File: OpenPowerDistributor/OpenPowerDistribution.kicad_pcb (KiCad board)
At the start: 2 copper layers, 16 parts, among them U1 AP63200WU, U2 LGS6302

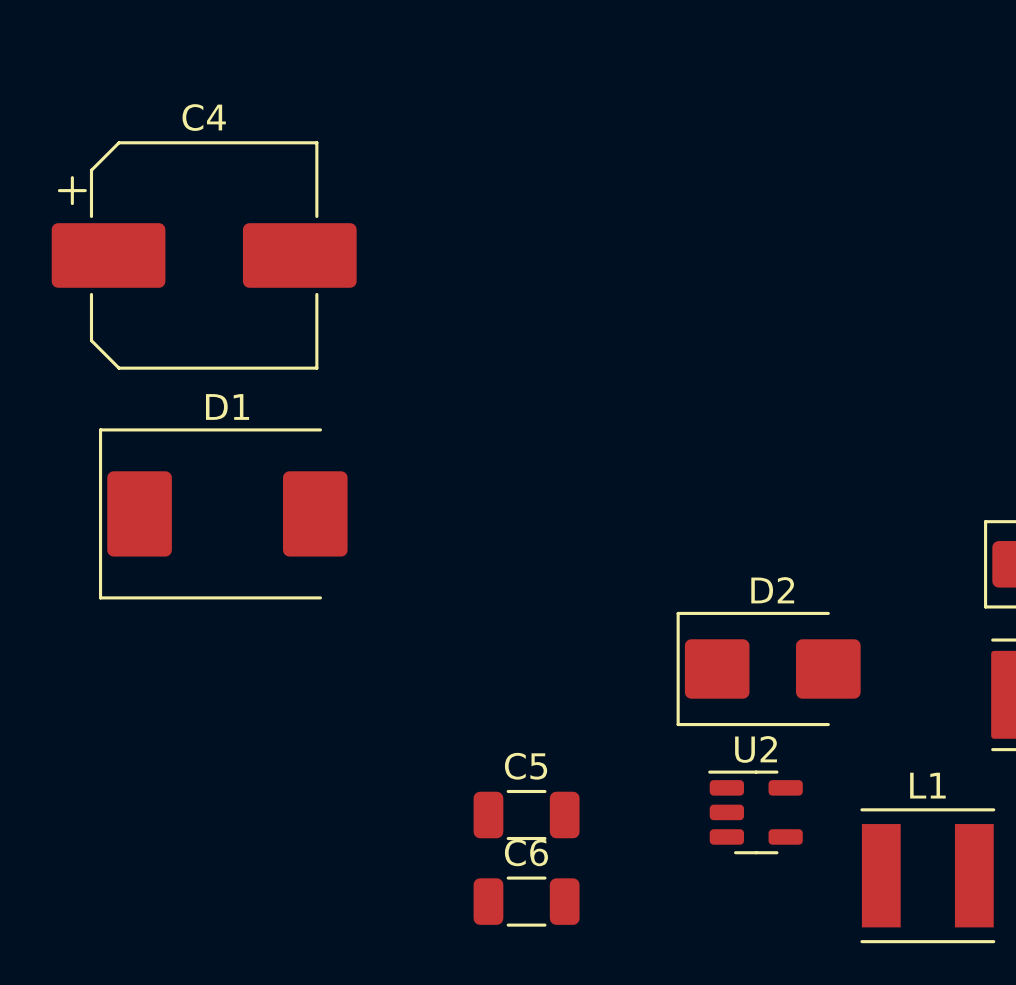
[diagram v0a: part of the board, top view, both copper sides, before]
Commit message: Added manual high side power switch
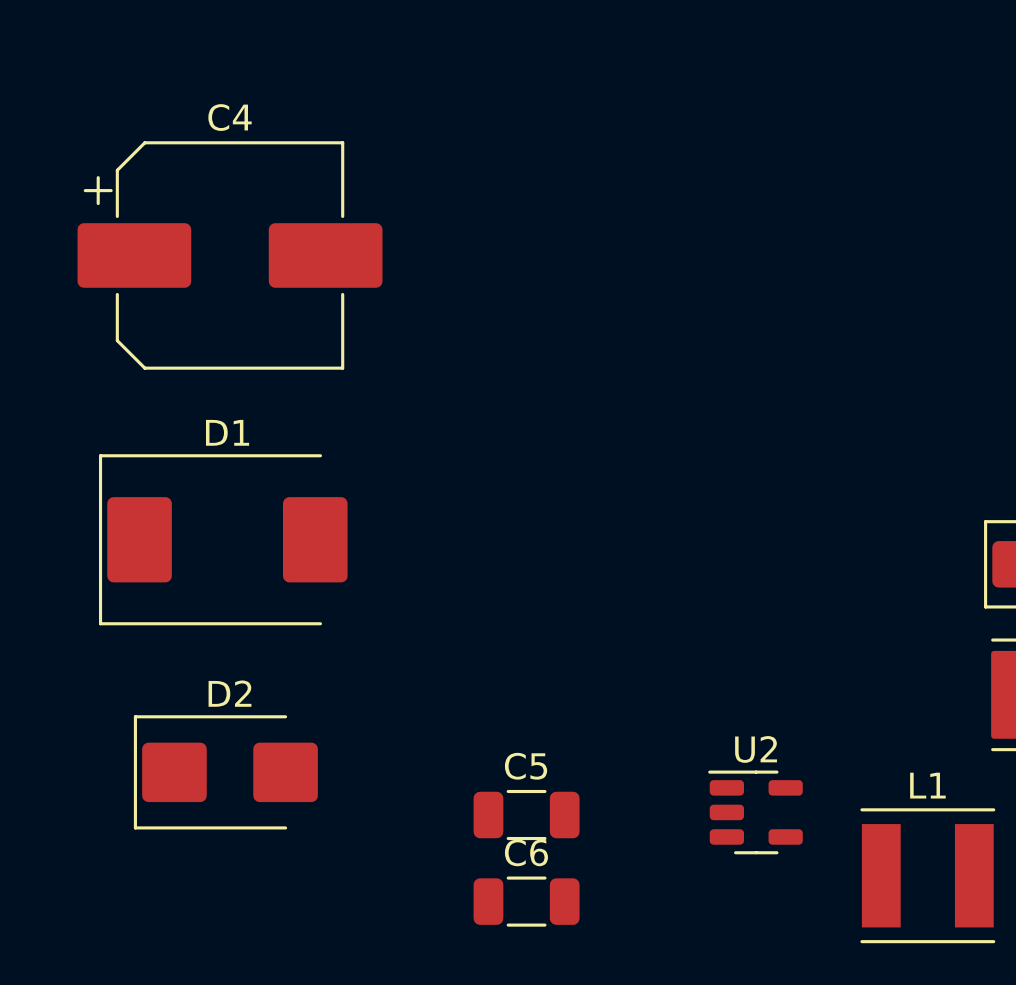
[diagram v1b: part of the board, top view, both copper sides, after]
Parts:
- moved D2 21.4 mm to (46.0, 60.0)
- moved C4 1.00 mm to (46.0, 40.0)
- moved D1 1.00 mm to (45.9, 51.0)
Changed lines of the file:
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@@
   (net 11 "+5V")
   (footprint "Diode_SMD:D_SMB" (layer "F.Cu")
-    (at 67 56)
+    (at 46 60)
     (descr "Diode SMB (DO-214AA)")
     (tags "Diode SMB (DO-214AA)")
@@
   )
   (footprint "Capacitor_SMD:CP_Elec_8x10.5" (layer "F.Cu")
-    (at 45 40)
+    (at 46 40)
     (descr "SMD capacitor, aluminum electrolytic, Vishay 0810, 8.0x10.5mm, http://www.vishay.com/docs/28395/150crz.pdf")
     (tags "capacitor electrolytic")
@@
   )
   (footprint "Diode_SMD:D_SMC" (layer "F.Cu")
-    (at 45.9 50)
+    (at 45.9 51)
     (descr "Diode SMC (DO-214AB)")
     (tags "Diode SMC (DO-214AB)")

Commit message: More schematic progress
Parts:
- added C10: 100nF 16V, Capacitor_SMD:C_0603_1608Metric, F.Cu at (-26.2, -64.5)
- added C11: 100nF 16V, Capacitor_SMD:C_0603_1608Metric, F.Cu at (-60.4, -53.8)
- added C12: NA, Capacitor_SMD:C_0603_1608Metric, F.Cu at (-60.4, -51.2)
- added C13: 100nF 16V, Capacitor_SMD:C_0603_1608Metric, F.Cu at (432.4, 46.4)
- added C14: 100nF 16V, Capacitor_SMD:C_0603_1608Metric, F.Cu at (432.4, 48.9)
- added C15: NA, Capacitor_SMD:C_0603_1608Metric, F.Cu at (432.4, 51.4)
- added C16: NA, Capacitor_SMD:C_0603_1608Metric, F.Cu at (432.4, 53.9)
- added C17: 100nF 16V, Capacitor_SMD:C_0603_1608Metric, F.Cu at (432.4, 56.4)
- added C18: 100nF 16V, Capacitor_SMD:C_0603_1608Metric, F.Cu at (468.5, 6.00)
- added C19: 100nF 16V, Capacitor_SMD:C_0603_1608Metric, F.Cu at (468.5, 8.51)
- added C20: NA, Capacitor_SMD:C_0603_1608Metric, F.Cu at (468.5, 11.0)
- added C21: NA, Capacitor_SMD:C_0603_1608Metric, F.Cu at (468.5, 13.5)
- added C22: 100nF 16V, Capacitor_SMD:C_0603_1608Metric, F.Cu at (468.5, 16.0)
- added C23: 100nF 16V, Capacitor_SMD:C_0603_1608Metric, F.Cu at (432.4, 6.00)
- added C24: 100nF 16V, Capacitor_SMD:C_0603_1608Metric, F.Cu at (432.4, 8.51)
- added C25: NA, Capacitor_SMD:C_0603_1608Metric, F.Cu at (432.4, 11.0)
- added C26: NA, Capacitor_SMD:C_0603_1608Metric, F.Cu at (432.4, 13.5)
- added C27: 100nF 16V, Capacitor_SMD:C_0603_1608Metric, F.Cu at (432.4, 16.0)
- added C28: 100nF 16V, Capacitor_SMD:C_0603_1608Metric, F.Cu at (391.6, 69.0)
- added C29: 100nF 16V, Capacitor_SMD:C_0603_1608Metric, F.Cu at (391.6, 71.5)
- added C30: NA, Capacitor_SMD:C_0603_1608Metric, F.Cu at (391.6, 74.0)
- added C31: NA, Capacitor_SMD:C_0603_1608Metric, F.Cu at (391.6, 76.5)
- added C32: 100nF 16V, Capacitor_SMD:C_0603_1608Metric, F.Cu at (391.6, 79.1)
- added C33: 100nF 16V, Capacitor_SMD:C_0603_1608Metric, F.Cu at (391.6, 25.6)
- added C34: 100nF 16V, Capacitor_SMD:C_0603_1608Metric, F.Cu at (391.6, 28.2)
- added C35: NA, Capacitor_SMD:C_0603_1608Metric, F.Cu at (391.6, 30.7)
- added C36: NA, Capacitor_SMD:C_0603_1608Metric, F.Cu at (391.6, 33.2)
- added C37: 100nF 16V, Capacitor_SMD:C_0603_1608Metric, F.Cu at (391.6, 35.7)
- added C38: 100nF 16V, Capacitor_SMD:C_0603_1608Metric, F.Cu at (432.4, 86.8)
- added C39: 100nF 16V, Capacitor_SMD:C_0603_1608Metric, F.Cu at (432.4, 89.3)
- added C40: NA, Capacitor_SMD:C_0603_1608Metric, F.Cu at (432.4, 91.8)
- added C41: NA, Capacitor_SMD:C_0603_1608Metric, F.Cu at (432.4, 94.3)
- added C42: 100nF 16V, Capacitor_SMD:C_0603_1608Metric, F.Cu at (432.4, 96.8)
- added C43: 100nF 16V, Capacitor_SMD:C_0603_1608Metric, F.Cu at (468.5, 46.4)
- added C44: 100nF 16V, Capacitor_SMD:C_0603_1608Metric, F.Cu at (468.5, 48.9)
- added C45: NA, Capacitor_SMD:C_0603_1608Metric, F.Cu at (468.5, 51.4)
- added C46: NA, Capacitor_SMD:C_0603_1608Metric, F.Cu at (468.5, 53.9)
- added C47: 100nF 16V, Capacitor_SMD:C_0603_1608Metric, F.Cu at (468.5, 56.4)
- added C48: 100nF 16V, Capacitor_SMD:C_0603_1608Metric, F.Cu at (391.6, 92.7)
- added C49: 100nF 16V, Capacitor_SMD:C_0603_1608Metric, F.Cu at (391.6, 95.2)
- added C50: NA, Capacitor_SMD:C_0603_1608Metric, F.Cu at (391.6, 97.8)
- added C51: NA, Capacitor_SMD:C_0603_1608Metric, F.Cu at (391.6, 100.3)
- added C52: 100nF 16V, Capacitor_SMD:C_0603_1608Metric, F.Cu at (391.6, 102.8)
- added C53: 10uF 50V, Capacitor_SMD:C_1206_3216Metric, F.Cu at (492.0, 14.6)
- added C54: 100nF 16V, Capacitor_SMD:C_0603_1608Metric, F.Cu at (492.6, 10.2)
- added C55: 47uF 16V, Capacitor_SMD:C_1210_3225Metric, F.Cu at (493.4, 6.87)
- added C57: 47uF 16V, Capacitor_SMD:C_1210_3225Metric, F.Cu at (473.7, 127.5)
- added C58: 100nF 16V, Capacitor_SMD:C_0603_1608Metric, F.Cu at (492.6, 26.9)
- added C59: 47uF 16V, Capacitor_SMD:C_1210_3225Metric, F.Cu at (493.4, 23.6)
- added C7: NA, Capacitor_SMD:C_0603_1608Metric, F.Cu at (125.5, 105.5)
- added C8: NA, Capacitor_SMD:C_0603_1608Metric, F.Cu at (-23.9, -59.7)
- added C9: 100nF 16V, Capacitor_SMD:C_0603_1608Metric, F.Cu at (118.7, 83.0)
- added D10: SS36(F), Diode_SMD:D_SMA, F.Cu at (-46.3, -42.6)
- added D11: SMAJ24A, Diode_SMD:D_SMA, F.Cu at (448.6, 96.9)
- added D12: SMAJ12A, Diode_SMD:D_SMA, F.Cu at (448.6, 101.4)
- added D13: SMAJ12A, Diode_SMD:D_SMA, F.Cu at (448.6, 106.0)
- added D14: AZ23C16, Package_TO_SOT_SMD:SOT-23, F.Cu at (428.0, 47.4)
- added D15: AZ23C16, Package_TO_SOT_SMD:SOT-23, F.Cu at (428.0, 51.8)
- added D16: SMAJ9.0A, Diode_SMD:D_SMA, F.Cu at (448.6, 110.5)
- added D17: SS36(F), Diode_SMD:D_SMA, F.Cu at (412.5, 72.7)
- added D18: SS36(F), Diode_SMD:D_SMA, F.Cu at (412.5, 77.2)
- added D19: SMAJ12A, Diode_SMD:D_SMA, F.Cu at (448.6, 115.1)
- added D20: SMAJ12A, Diode_SMD:D_SMA, F.Cu at (456.7, 87.8)
- added D21: AZ23C16, Package_TO_SOT_SMD:SOT-23, F.Cu at (464.1, 6.96)
- added D22: AZ23C16, Package_TO_SOT_SMD:SOT-23, F.Cu at (464.1, 11.4)
- added D23: SMAJ9.0A, Diode_SMD:D_SMA, F.Cu at (456.7, 92.3)
- added D24: SS36(F), Diode_SMD:D_SMA, F.Cu at (448.6, 32.3)
- added D25: SS36(F), Diode_SMD:D_SMA, F.Cu at (448.6, 36.8)
- added D26: SMAJ12A, Diode_SMD:D_SMA, F.Cu at (456.7, 96.9)
- added D27: SMAJ12A, Diode_SMD:D_SMA, F.Cu at (456.7, 101.4)
- added D28: AZ23C16, Package_TO_SOT_SMD:SOT-23, F.Cu at (428.0, 6.96)
- added D29: AZ23C16, Package_TO_SOT_SMD:SOT-23, F.Cu at (428.0, 11.4)
- added D30: SMAJ9.0A, Diode_SMD:D_SMA, F.Cu at (456.7, 106.0)
- added D31: SS36(F), Diode_SMD:D_SMA, F.Cu at (412.5, 32.3)
- added D32: SS36(F), Diode_SMD:D_SMA, F.Cu at (412.5, 36.8)
- added D33: SMAJ5.0A, Diode_SMD:D_SMA, F.Cu at (456.7, 110.5)
- added D34: SMAJ5.0A, Diode_SMD:D_SMA, F.Cu at (456.7, 115.1)
- added D35: SMAJ5.0A, Diode_SMD:D_SMA, F.Cu at (464.8, 87.8)
- added D36: SMAJ5.0A, Diode_SMD:D_SMA, F.Cu at (464.8, 92.3)
- added D37: SMAJ5.0A, Diode_SMD:D_SMA, F.Cu at (464.8, 96.9)
- added D38: SMAJ5.0A, Diode_SMD:D_SMA, F.Cu at (464.8, 101.4)
- added D39: AZ23C16, Package_TO_SOT_SMD:SOT-23, F.Cu at (370.1, 50.3)
- added D40: AZ23C16, Package_TO_SOT_SMD:SOT-23, F.Cu at (370.1, 54.8)
- added D41: AZ23C16, Package_TO_SOT_SMD:SOT-23, F.Cu at (447.0, 47.4)
- added D42: SS36(F), Diode_SMD:D_SMA, F.Cu at (402.5, 50.4)
- added D43: SS36(F), Diode_SMD:D_SMA, F.Cu at (402.5, 54.9)
- added D44: AZ23C16, Package_TO_SOT_SMD:SOT-23, F.Cu at (370.1, 6.96)
- added D45: AZ23C16, Package_TO_SOT_SMD:SOT-23, F.Cu at (370.1, 11.4)
- added D46: AZ23C16, Package_TO_SOT_SMD:SOT-23, F.Cu at (447.0, 51.8)
- added D47: SS36(F), Diode_SMD:D_SMA, F.Cu at (402.5, 7.01)
- added D48: SS36(F), Diode_SMD:D_SMA, F.Cu at (402.5, 11.6)
- added D49: AZ23C16, Package_TO_SOT_SMD:SOT-23, F.Cu at (428.0, 87.8)
- added D5: SS36(F), Diode_SMD:D_SMA, F.Cu at (-26.1, -80.0)
- added D50: AZ23C16, Package_TO_SOT_SMD:SOT-23, F.Cu at (428.0, 92.2)
- added D51: SS36(F), Diode_SMD:D_SMA, F.Cu at (462.3, 72.7)
- added D52: SS36(F), Diode_SMD:D_SMA, F.Cu at (412.5, 113.1)
- added D53: SS36(F), Diode_SMD:D_SMA, F.Cu at (412.5, 117.6)
- added D54: SS36(F), Diode_SMD:D_SMA, F.Cu at (462.3, 77.2)
- added D55: AZ23C16, Package_TO_SOT_SMD:SOT-23, F.Cu at (387.2, 93.7)
- added D56: AZ23C16, Package_TO_SOT_SMD:SOT-23, F.Cu at (387.2, 98.2)
- added D57: SS36(F), Diode_SMD:D_SMA, F.Cu at (371.8, 119.0)
- added D58: SS36(F), Diode_SMD:D_SMA, F.Cu at (371.8, 123.6)
- added D6: AZ23C16, Package_TO_SOT_SMD:SOT-23, F.Cu at (490.3, 87.7)
- added D7: SMAJ24A, Diode_SMD:D_SMA, F.Cu at (448.6, 87.8)
- added D8: AZ23C16, Package_TO_SOT_SMD:SOT-23, F.Cu at (-31.9, -80.0)
- added D9: SMAJ9.0A, Diode_SMD:D_SMA, F.Cu at (448.6, 92.3)
- added J1: Barrel_Jack, Connector_BarrelJack:BarrelJack_Horizontal, F.Cu at (485.4, 118.1)
- added J10: Barrel_Jack, Connector_BarrelJack:BarrelJack_Horizontal, F.Cu at (387.1, 53.5)
- added J11: Barrel_Jack, Connector_BarrelJack:BarrelJack_Horizontal, F.Cu at (387.1, 66.1)
- added J12: Barrel_Jack, Connector_BarrelJack:BarrelJack_Horizontal, F.Cu at (387.1, 10.1)
- added J13: Barrel_Jack, Connector_BarrelJack:BarrelJack_Horizontal, F.Cu at (387.1, 22.7)
- added J14: Barrel_Jack, Connector_BarrelJack:BarrelJack_Horizontal, F.Cu at (423.0, 90.9)
- added J15: Barrel_Jack, Connector_BarrelJack:BarrelJack_Horizontal, F.Cu at (423.0, 103.5)
- added J16: Barrel_Jack, Connector_BarrelJack:BarrelJack_Horizontal, F.Cu at (464.0, 50.5)
- added J17: Barrel_Jack, Connector_BarrelJack:BarrelJack_Horizontal, F.Cu at (464.0, 63.1)
- added J18: Barrel_Jack, Connector_BarrelJack:BarrelJack_Horizontal, F.Cu at (382.2, 96.8)
- added J19: Barrel_Jack, Connector_BarrelJack:BarrelJack_Horizontal, F.Cu at (382.2, 109.5)
- added J2: Barrel_Jack, Connector_BarrelJack:BarrelJack_Horizontal, F.Cu at (-36.5, -75.2)
- added J3: Barrel_Jack, Connector_BarrelJack:BarrelJack_Horizontal, F.Cu at (485.4, 103.5)
- added J4: Barrel_Jack, Connector_BarrelJack:BarrelJack_Horizontal, F.Cu at (423.0, 50.5)
- added J5: Barrel_Jack, Connector_BarrelJack:BarrelJack_Horizontal, F.Cu at (423.0, 63.1)
- added J6: Barrel_Jack, Connector_BarrelJack:BarrelJack_Horizontal, F.Cu at (459.1, 10.1)
- added J7: Barrel_Jack, Connector_BarrelJack:BarrelJack_Horizontal, F.Cu at (459.1, 22.7)
- added J8: Barrel_Jack, Connector_BarrelJack:BarrelJack_Horizontal, F.Cu at (423.0, 10.1)
- added J9: Barrel_Jack, Connector_BarrelJack:BarrelJack_Horizontal, F.Cu at (423.0, 22.7)
- added L3: 3.3uH, Inductor_SMD:L_Bourns_SRP7028A_7.3x6.6mm, F.Cu at (485.6, 8.81)
- added L4: 3.3uH, Inductor_SMD:L_Bourns_SRP7028A_7.3x6.6mm, F.Cu at (485.6, 25.5)
- added Q1: STN2610D, Package_TO_SOT_SMD:TO-252-2, F.Cu at (-26.2, -74.5)
- added Q10: BC847, Package_TO_SOT_SMD:SOT-23, F.Cu at (428.0, 69.6)
- added Q11: STN2610D, Package_TO_SOT_SMD:TO-252-2, F.Cu at (437.3, 66.7)
- added Q12: STN2610D, Package_TO_SOT_SMD:TO-252-2, F.Cu at (437.3, 74.8)
- added Q13: BC847, Package_TO_SOT_SMD:SOT-23, F.Cu at (464.1, 15.9)
- added Q14: BC847, Package_TO_SOT_SMD:SOT-23, F.Cu at (464.1, 20.3)
- added Q15: BC847, Package_TO_SOT_SMD:SOT-23, F.Cu at (464.1, 24.8)
- added Q16: BC847, Package_TO_SOT_SMD:SOT-23, F.Cu at (464.1, 29.2)
- added Q17: STN2610D, Package_TO_SOT_SMD:TO-252-2, F.Cu at (473.4, 26.3)
- added Q18: STN2610D, Package_TO_SOT_SMD:TO-252-2, F.Cu at (473.4, 34.4)
- added Q19: BC847, Package_TO_SOT_SMD:SOT-23, F.Cu at (428.0, 15.9)
- added Q2: BC847, Package_TO_SOT_SMD:SOT-23, F.Cu at (-30.6, -61.3)
- added Q20: BC847, Package_TO_SOT_SMD:SOT-23, F.Cu at (428.0, 20.3)
- added Q21: BC847, Package_TO_SOT_SMD:SOT-23, F.Cu at (428.0, 24.8)
- added Q22: BC847, Package_TO_SOT_SMD:SOT-23, F.Cu at (428.0, 29.2)
- added Q23: STN2610D, Package_TO_SOT_SMD:TO-252-2, F.Cu at (437.3, 26.3)
- added Q24: STN2610D, Package_TO_SOT_SMD:TO-252-2, F.Cu at (437.3, 34.4)
- added Q25: BC847, Package_TO_SOT_SMD:SOT-23, F.Cu at (370.1, 59.2)
- added Q26: BC847, Package_TO_SOT_SMD:SOT-23, F.Cu at (370.1, 63.7)
- added Q27: BC847, Package_TO_SOT_SMD:SOT-23, F.Cu at (370.1, 68.1)
- added Q28: BC847, Package_TO_SOT_SMD:SOT-23, F.Cu at (370.1, 72.6)
- added Q29: STN2610D, Package_TO_SOT_SMD:TO-252-2, F.Cu at (379.5, 77.4)
- added Q3: BC847, Package_TO_SOT_SMD:SOT-23, F.Cu at (-14.3, -71.9)
- added Q30: STN2610D, Package_TO_SOT_SMD:TO-252-2, F.Cu at (379.5, 85.5)
- added Q31: BC847, Package_TO_SOT_SMD:SOT-23, F.Cu at (370.1, 15.9)
- added Q32: BC847, Package_TO_SOT_SMD:SOT-23, F.Cu at (370.1, 20.3)
- added Q33: BC847, Package_TO_SOT_SMD:SOT-23, F.Cu at (370.1, 24.8)
- added Q34: BC847, Package_TO_SOT_SMD:SOT-23, F.Cu at (370.1, 29.2)
- added Q35: STN2610D, Package_TO_SOT_SMD:TO-252-2, F.Cu at (379.5, 34.0)
- added Q36: STN2610D, Package_TO_SOT_SMD:TO-252-2, F.Cu at (379.5, 42.1)
- added Q37: BC847, Package_TO_SOT_SMD:SOT-23, F.Cu at (428.0, 96.7)
- added Q38: BC847, Package_TO_SOT_SMD:SOT-23, F.Cu at (428.0, 101.1)
- added Q39: BC847, Package_TO_SOT_SMD:SOT-23, F.Cu at (428.0, 105.6)
- added Q4: BC847, Package_TO_SOT_SMD:SOT-23, F.Cu at (-39.8, -47.2)
- added Q40: BC847, Package_TO_SOT_SMD:SOT-23, F.Cu at (428.0, 110.0)
- added Q41: STN2610D, Package_TO_SOT_SMD:TO-252-2, F.Cu at (437.3, 107.1)
- added Q42: STN2610D, Package_TO_SOT_SMD:TO-252-2, F.Cu at (437.3, 115.2)
- added Q43: BC847, Package_TO_SOT_SMD:SOT-23, F.Cu at (447.0, 56.3)
- added Q44: BC847, Package_TO_SOT_SMD:SOT-23, F.Cu at (447.0, 60.7)
- added Q45: BC847, Package_TO_SOT_SMD:SOT-23, F.Cu at (447.0, 65.2)
- added Q46: BC847, Package_TO_SOT_SMD:SOT-23, F.Cu at (447.0, 69.6)
- added Q47: STN2610D, Package_TO_SOT_SMD:TO-252-2, F.Cu at (473.4, 66.7)
- added Q48: STN2610D, Package_TO_SOT_SMD:TO-252-2, F.Cu at (473.4, 74.8)
- added Q49: BC847, Package_TO_SOT_SMD:SOT-23, F.Cu at (387.2, 102.6)
- added Q5: BC847, Package_TO_SOT_SMD:SOT-23, F.Cu at (-39.8, -42.8)
- added Q50: BC847, Package_TO_SOT_SMD:SOT-23, F.Cu at (387.2, 107.1)
- added Q51: BC847, Package_TO_SOT_SMD:SOT-23, F.Cu at (387.2, 111.5)
- added Q52: BC847, Package_TO_SOT_SMD:SOT-23, F.Cu at (387.2, 116.0)
- added Q53: STN2610D, Package_TO_SOT_SMD:TO-252-2, F.Cu at (396.6, 113.1)
- added Q54: STN2610D, Package_TO_SOT_SMD:TO-252-2, F.Cu at (396.6, 121.1)
- added Q6: STN2610D, Package_TO_SOT_SMD:TO-252-2, F.Cu at (-43.4, -53.5)
- added Q7: BC847, Package_TO_SOT_SMD:SOT-23, F.Cu at (428.0, 56.3)
- added Q8: BC847, Package_TO_SOT_SMD:SOT-23, F.Cu at (428.0, 60.7)
- added Q9: BC847, Package_TO_SOT_SMD:SOT-23, F.Cu at (428.0, 65.2)
- added R10: 1M, Resistor_SMD:R_0603_1608Metric, F.Cu at (-27.8, -64.6)
- added R100: 1M, Resistor_SMD:R_0603_1608Metric, F.Cu at (395.6, 33.2)
- added R101: 1M, Resistor_SMD:R_0603_1608Metric, F.Cu at (395.6, 35.7)
- added R102: 100k, Resistor_SMD:R_0603_1608Metric, F.Cu at (395.6, 38.2)
- added R103: 1M, Resistor_SMD:R_0603_1608Metric, F.Cu at (395.6, 40.7)
- added R104: 100k, Resistor_SMD:R_0603_1608Metric, F.Cu at (399.7, 25.6)
- added R105: 390k, Resistor_SMD:R_0603_1608Metric, F.Cu at (399.7, 28.2)
- added R106: 390k, Resistor_SMD:R_0603_1608Metric, F.Cu at (399.7, 30.7)
- added R107: 15k, Resistor_SMD:R_0603_1608Metric, F.Cu at (399.7, 33.2)
- added R108: 15k, Resistor_SMD:R_0603_1608Metric, F.Cu at (399.7, 35.7)
- added R109: 33mR, Resistor_SMD:R_1206_3216Metric, F.Cu at (401.2, 15.5)
- added R11: 100k, Resistor_SMD:R_0603_1608Metric, F.Cu at (-33.5, -72.5)
- added R110: 33mR, Resistor_SMD:R_1206_3216Metric, F.Cu at (401.2, 18.8)
- added R111: 100k, Resistor_SMD:R_0603_1608Metric, F.Cu at (399.7, 38.2)
- added R112: 100k, Resistor_SMD:R_0603_1608Metric, F.Cu at (399.7, 40.7)
- added R113: 390k, Resistor_SMD:R_0603_1608Metric, F.Cu at (432.4, 99.3)
- added R114: 390k, Resistor_SMD:R_0603_1608Metric, F.Cu at (432.4, 101.9)
- added R115: 100k, Resistor_SMD:R_0603_1608Metric, F.Cu at (436.4, 86.8)
- added R116: 390k, Resistor_SMD:R_0603_1608Metric, F.Cu at (436.4, 89.3)
- added R117: 1M, Resistor_SMD:R_0603_1608Metric, F.Cu at (436.4, 91.8)
- added R118: 1M, Resistor_SMD:R_0603_1608Metric, F.Cu at (436.4, 94.3)
- added R119: 1M, Resistor_SMD:R_0603_1608Metric, F.Cu at (436.4, 96.8)
- added R12: 100k, Resistor_SMD:R_0603_1608Metric, F.Cu at (-14.3, -74.4)
- added R120: 100k, Resistor_SMD:R_0603_1608Metric, F.Cu at (436.4, 99.3)
- added R121: 1M, Resistor_SMD:R_0603_1608Metric, F.Cu at (436.4, 101.9)
- added R122: 100k, Resistor_SMD:R_0603_1608Metric, F.Cu at (440.4, 86.8)
- added R123: 390k, Resistor_SMD:R_0603_1608Metric, F.Cu at (440.4, 89.3)
- added R124: 390k, Resistor_SMD:R_0603_1608Metric, F.Cu at (440.4, 91.8)
- added R125: 15k, Resistor_SMD:R_0603_1608Metric, F.Cu at (440.4, 94.3)
- added R126: 15k, Resistor_SMD:R_0603_1608Metric, F.Cu at (440.4, 96.8)
- added R127: 33mR, Resistor_SMD:R_1206_3216Metric, F.Cu at (419.4, 119.0)
- added R128: 33mR, Resistor_SMD:R_1206_3216Metric, F.Cu at (419.4, 122.3)
- added R129: 100k, Resistor_SMD:R_0603_1608Metric, F.Cu at (440.4, 99.3)
- added R13: 390k, Resistor_SMD:R_0603_1608Metric, F.Cu at (-27.1, -66.9)
- added R130: 100k, Resistor_SMD:R_0603_1608Metric, F.Cu at (440.4, 101.9)
- added R131: 390k, Resistor_SMD:R_0603_1608Metric, F.Cu at (468.5, 58.9)
- added R132: 390k, Resistor_SMD:R_0603_1608Metric, F.Cu at (468.5, 61.5)
- added R133: 100k, Resistor_SMD:R_0603_1608Metric, F.Cu at (472.5, 46.4)
- added R134: 390k, Resistor_SMD:R_0603_1608Metric, F.Cu at (472.5, 48.9)
- added R135: 1M, Resistor_SMD:R_0603_1608Metric, F.Cu at (472.5, 51.4)
- added R136: 1M, Resistor_SMD:R_0603_1608Metric, F.Cu at (472.5, 53.9)
- added R137: 1M, Resistor_SMD:R_0603_1608Metric, F.Cu at (472.5, 56.4)
- added R138: 100k, Resistor_SMD:R_0603_1608Metric, F.Cu at (472.5, 58.9)
- added R139: 1M, Resistor_SMD:R_0603_1608Metric, F.Cu at (472.5, 61.5)
- added R14: 390k, Resistor_SMD:R_0603_1608Metric, F.Cu at (-56.4, -46.2)
- added R140: 100k, Resistor_SMD:R_0603_1608Metric, F.Cu at (476.5, 46.4)
- added R141: 390k, Resistor_SMD:R_0603_1608Metric, F.Cu at (476.5, 48.9)
- added R142: 390k, Resistor_SMD:R_0603_1608Metric, F.Cu at (476.5, 51.4)
- added R143: 15k, Resistor_SMD:R_0603_1608Metric, F.Cu at (476.5, 53.9)
- added R144: 15k, Resistor_SMD:R_0603_1608Metric, F.Cu at (476.5, 56.4)
- added R145: 33mR, Resistor_SMD:R_1206_3216Metric, F.Cu at (481.3, 46.8)
- added R146: 33mR, Resistor_SMD:R_1206_3216Metric, F.Cu at (481.3, 50.1)
- added R147: 100k, Resistor_SMD:R_0603_1608Metric, F.Cu at (476.5, 58.9)
- added R148: 100k, Resistor_SMD:R_0603_1608Metric, F.Cu at (476.5, 61.5)
- added R149: 390k, Resistor_SMD:R_0603_1608Metric, F.Cu at (391.6, 105.3)
- added R15: 390k, Resistor_SMD:R_0603_1608Metric, F.Cu at (-56.4, -43.7)
- added R150: 390k, Resistor_SMD:R_0603_1608Metric, F.Cu at (391.6, 107.8)
- added R151: 100k, Resistor_SMD:R_0603_1608Metric, F.Cu at (395.6, 92.7)
- added R152: 390k, Resistor_SMD:R_0603_1608Metric, F.Cu at (395.6, 95.2)
- added R153: 1M, Resistor_SMD:R_0603_1608Metric, F.Cu at (395.6, 97.8)
- added R154: 1M, Resistor_SMD:R_0603_1608Metric, F.Cu at (395.6, 100.3)
- added R155: 1M, Resistor_SMD:R_0603_1608Metric, F.Cu at (395.6, 102.8)
- added R156: 100k, Resistor_SMD:R_0603_1608Metric, F.Cu at (395.6, 105.3)
- added R157: 1M, Resistor_SMD:R_0603_1608Metric, F.Cu at (395.6, 107.8)
- added R158: 100k, Resistor_SMD:R_0603_1608Metric, F.Cu at (399.7, 92.7)
- added R159: 390k, Resistor_SMD:R_0603_1608Metric, F.Cu at (399.7, 95.2)
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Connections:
- C4 pad 1: +12V -> GND
- C4 pad 2: GND -> Net-(U18-VREG5)

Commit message: More work on schematic wiring
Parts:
- removed U14, U15, U16: LM324, Package_SO:TSSOP-14_4.4x5mm_P0.65mm
- added D59: AZ23C16, Package_TO_SOT_SMD:SOT-23, F.Cu at (81.1, -26.3)
- added D60: AZ23C16, Package_TO_SOT_SMD:SOT-23, F.Cu at (81.1, -21.9)
- added D61: SS36(F), Diode_SMD:D_SMA, F.Cu at (87.6, -0.98)
- added D62: SS36(F), Diode_SMD:D_SMA, F.Cu at (87.6, 3.57)
- added D63: Red, LED_SMD:LED_0603_1608Metric, F.Cu at (114.8, -9.66)
- added D64: Green, LED_SMD:LED_0603_1608Metric, F.Cu at (114.8, -7.07)
- added D65: Red, LED_SMD:LED_0603_1608Metric, F.Cu at (114.8, -4.48)
- added D66: Green, LED_SMD:LED_0603_1608Metric, F.Cu at (114.8, -1.89)
- added D67: SMAJ12A, Diode_SMD:D_SMA, F.Cu at (166.7, 37.0)
- added D68: SMAJ12A, Diode_SMD:D_SMA, F.Cu at (174.8, 9.71)
- added D69: AZ23C16, Package_TO_SOT_SMD:SOT-23, F.Cu at (81.1, 10.1)
- added D7: SS36(F), Diode_SMD:D_SMA, F.Cu at (-207.7, -62.5)
- added D70: AZ23C16, Package_TO_SOT_SMD:SOT-23, F.Cu at (81.1, 14.5)
- added D71: SS36(F), Diode_SMD:D_SMA, F.Cu at (87.6, 35.4)
- added D72: SS36(F), Diode_SMD:D_SMA, F.Cu at (87.6, 39.9)
- added D73: Red, LED_SMD:LED_0603_1608Metric, F.Cu at (114.8, 26.7)
- added D74: Green, LED_SMD:LED_0603_1608Metric, F.Cu at (114.8, 29.3)
- added D75: Red, LED_SMD:LED_0603_1608Metric, F.Cu at (114.8, 31.9)
- added D76: Green, LED_SMD:LED_0603_1608Metric, F.Cu at (114.8, 34.5)
- added D77: SMAJ24A, Diode_SMD:D_SMA, F.Cu at (174.8, 14.3)
- added D78: SMAJ24A, Diode_SMD:D_SMA, F.Cu at (174.8, 18.8)
- added D79: SMAJ12A, Diode_SMD:D_SMA, F.Cu at (174.8, 23.4)
- added D80: SMAJ12A, Diode_SMD:D_SMA, F.Cu at (174.8, 27.9)
- added D81: AZ23C16, Package_TO_SOT_SMD:SOT-23, F.Cu at (124.9, 9.66)
- added D82: AZ23C16, Package_TO_SOT_SMD:SOT-23, F.Cu at (124.9, 14.1)
- added D83: SS36(F), Diode_SMD:D_SMA, F.Cu at (131.5, 35.0)
- added D84: SS36(F), Diode_SMD:D_SMA, F.Cu at (131.5, 39.5)
- added D85: SMAJ5.0A, Diode_SMD:D_SMA, F.Cu at (174.8, 32.5)
- added D86: SMAJ5.0A, Diode_SMD:D_SMA, F.Cu at (174.8, 37.0)
- added D87: Red, LED_SMD:LED_0603_1608Metric, F.Cu at (158.6, 26.3)
- added D88: Green, LED_SMD:LED_0603_1608Metric, F.Cu at (158.6, 28.9)
- added D89: Red, LED_SMD:LED_0603_1608Metric, F.Cu at (158.6, 31.5)
- added D90: Green, LED_SMD:LED_0603_1608Metric, F.Cu at (158.6, 34.1)
- added D91: SMAJ9.0A, Diode_SMD:D_SMA, F.Cu at (182.9, 9.71)
- added D92: SMAJ9.0A, Diode_SMD:D_SMA, F.Cu at (182.9, 14.3)
- added D93: SMAJ9.0A, Diode_SMD:D_SMA, F.Cu at (182.9, 18.8)
- added D94: SMAJ9.0A, Diode_SMD:D_SMA, F.Cu at (182.9, 23.4)
- added FB1: 220R@100MHz 3A, Inductor_SMD:L_0805_2012Metric, F.Cu at (115.7, -65.4)
- added FB2: 220R@100MHz 3A, Inductor_SMD:L_0805_2012Metric, F.Cu at (-21.1, -67.5)
- added FB3: 220R@100MHz 3A, Inductor_SMD:L_0805_2012Metric, F.Cu at (169.8, 2.78)
- added FB4: 220R@100MHz 3A, Inductor_SMD:L_0805_2012Metric, F.Cu at (129.7, -37.6)
- added FB5: 220R@100MHz 3A, Inductor_SMD:L_0805_2012Metric, F.Cu at (129.7, 2.78)
- added FB6: 220R@100MHz 3A, Inductor_SMD:L_0805_2012Metric, F.Cu at (169.8, -37.6)
- added FB7: 220R@100MHz 3A, Inductor_SMD:L_0805_2012Metric, F.Cu at (80.9, -0.45)
- added FB8: 220R@100MHz 3A, Inductor_SMD:L_0805_2012Metric, F.Cu at (80.9, 35.9)
- added FB9: 220R@100MHz 3A, Inductor_SMD:L_0805_2012Metric, F.Cu at (129.7, 43.2)
- added R171: 100k, Resistor_SMD:R_0603_1608Metric, F.Cu at (114.6, -27.3)
- added R172: 100k, Resistor_SMD:R_0603_1608Metric, F.Cu at (114.6, -24.8)
- added R173: 150R, Resistor_SMD:R_0603_1608Metric, F.Cu at (114.6, -22.2)
- added R174: 150R, Resistor_SMD:R_0603_1608Metric, F.Cu at (114.6, -19.7)
- added R175: 150R, Resistor_SMD:R_0603_1608Metric, F.Cu at (114.6, -17.2)
- added R176: 150R, Resistor_SMD:R_0603_1608Metric, F.Cu at (114.6, -14.7)
- added R177: 390k, Resistor_SMD:R_0603_1608Metric, F.Cu at (102.6, 21.6)
- added R178: 390k, Resistor_SMD:R_0603_1608Metric, F.Cu at (102.6, 24.2)
- added R179: 15k, Resistor_SMD:R_0603_1608Metric, F.Cu at (106.6, 9.10)
- added R180: 15k, Resistor_SMD:R_0603_1608Metric, F.Cu at (106.6, 11.6)
- added R181: 100k, Resistor_SMD:R_0603_1608Metric, F.Cu at (106.6, 14.1)
- added R182: 100k, Resistor_SMD:R_0603_1608Metric, F.Cu at (106.6, 16.6)
- added R183: 1M, Resistor_SMD:R_0603_1608Metric, F.Cu at (106.6, 19.1)
- added R184: 1M, Resistor_SMD:R_0603_1608Metric, F.Cu at (106.6, 21.6)
- added R185: 1M, Resistor_SMD:R_0603_1608Metric, F.Cu at (106.6, 24.2)
- added R186: 33k, Resistor_SMD:R_0603_1608Metric, F.Cu at (110.6, 9.10)
- added R187: 1M, Resistor_SMD:R_0603_1608Metric, F.Cu at (110.6, 11.6)
- added R188: 33k, Resistor_SMD:R_0603_1608Metric, F.Cu at (110.6, 14.1)
- added R189: 390k, Resistor_SMD:R_0603_1608Metric, F.Cu at (110.6, 16.6)
- added R190: 390k, Resistor_SMD:R_0603_1608Metric, F.Cu at (110.6, 19.1)
- added R191: 10k, Resistor_SMD:R_0603_1608Metric, F.Cu at (110.6, 21.6)
- added R192: 10k, Resistor_SMD:R_0603_1608Metric, F.Cu at (110.6, 24.2)
- added R193: 33mR, Resistor_SMD:R_1206_3216Metric, F.Cu at (94.5, 34.8)
- added R194: 33mR, Resistor_SMD:R_1206_3216Metric, F.Cu at (94.5, 38.0)
- added R195: 100k, Resistor_SMD:R_0603_1608Metric, F.Cu at (114.6, 9.10)
- added R196: 100k, Resistor_SMD:R_0603_1608Metric, F.Cu at (114.6, 11.6)
- added R197: 150R, Resistor_SMD:R_0603_1608Metric, F.Cu at (114.6, 14.1)
- added R198: 150R, Resistor_SMD:R_0603_1608Metric, F.Cu at (114.6, 16.6)
- added R199: 150R, Resistor_SMD:R_0603_1608Metric, F.Cu at (114.6, 19.1)
- added R200: 150R, Resistor_SMD:R_0603_1608Metric, F.Cu at (114.6, 21.6)
- added R201: 390k, Resistor_SMD:R_0603_1608Metric, F.Cu at (146.4, 21.2)
- added R202: 390k, Resistor_SMD:R_0603_1608Metric, F.Cu at (146.4, 23.8)
- added R203: 15k, Resistor_SMD:R_0603_1608Metric, F.Cu at (150.5, 8.69)
- added R204: 15k, Resistor_SMD:R_0603_1608Metric, F.Cu at (150.5, 11.2)
- added R205: 100k, Resistor_SMD:R_0603_1608Metric, F.Cu at (150.5, 13.7)
- added R206: 100k, Resistor_SMD:R_0603_1608Metric, F.Cu at (150.5, 16.2)
- added R207: 1M, Resistor_SMD:R_0603_1608Metric, F.Cu at (150.5, 18.7)
- added R208: 1M, Resistor_SMD:R_0603_1608Metric, F.Cu at (150.5, 21.2)
- added R209: 1M, Resistor_SMD:R_0603_1608Metric, F.Cu at (150.5, 23.8)
- added R210: 33k, Resistor_SMD:R_0603_1608Metric, F.Cu at (154.5, 8.69)
- added R211: 1M, Resistor_SMD:R_0603_1608Metric, F.Cu at (154.5, 11.2)
- added R212: 33k, Resistor_SMD:R_0603_1608Metric, F.Cu at (154.5, 13.7)
- added R213: 390k, Resistor_SMD:R_0603_1608Metric, F.Cu at (154.5, 16.2)
- added R214: 390k, Resistor_SMD:R_0603_1608Metric, F.Cu at (154.5, 18.7)
- added R215: 10k, Resistor_SMD:R_0603_1608Metric, F.Cu at (154.5, 21.2)
- added R216: 10k, Resistor_SMD:R_0603_1608Metric, F.Cu at (154.5, 23.8)
- added R217: 33mR, Resistor_SMD:R_1206_3216Metric, F.Cu at (138.3, 40.9)
- added R218: 33mR, Resistor_SMD:R_1206_3216Metric, F.Cu at (138.3, 44.2)
- added R219: 100k, Resistor_SMD:R_0603_1608Metric, F.Cu at (158.5, 8.69)
- added R220: 100k, Resistor_SMD:R_0603_1608Metric, F.Cu at (158.5, 11.2)
- added R221: 150R, Resistor_SMD:R_0603_1608Metric, F.Cu at (158.5, 13.7)
- added R222: 150R, Resistor_SMD:R_0603_1608Metric, F.Cu at (158.5, 16.2)
- added R223: 150R, Resistor_SMD:R_0603_1608Metric, F.Cu at (158.5, 18.7)
- added R224: 150R, Resistor_SMD:R_0603_1608Metric, F.Cu at (158.5, 21.2)
- C10, C11: value 100nF 16V -> NA
- C12, C8: value NA -> 100nF 16V
- D10, D32, D42, D48, D54: value SS36(F) -> Green; footprint Diode_SMD:D_SMA -> LED_SMD:LED_0603_1608Metric
- D11: value SMAJ24A -> Red; footprint Diode_SMD:D_SMA -> LED_SMD:LED_0603_1608Metric
- D12, D20: value SMAJ12A -> Green; footprint Diode_SMD:D_SMA -> LED_SMD:LED_0603_1608Metric
- D13: value SMAJ12A -> SMAJ5.0A
- D14: value AZ23C16 -> SMAJ5.0A; footprint Package_TO_SOT_SMD:SOT-23 -> Diode_SMD:D_SMA
- D16: value SMAJ9.0A -> AZ23C16; footprint Diode_SMD:D_SMA -> Package_TO_SOT_SMD:SOT-23
- D19: value SMAJ12A -> Red; footprint Diode_SMD:D_SMA -> LED_SMD:LED_0603_1608Metric
- D21, D29, D41, D45, D55: value AZ23C16 -> Red; footprint Package_TO_SOT_SMD:SOT-23 -> LED_SMD:LED_0603_1608Metric
- D22, D44, D46, D56: value AZ23C16 -> Green; footprint Package_TO_SOT_SMD:SOT-23 -> LED_SMD:LED_0603_1608Metric
- D23: value SMAJ9.0A -> SMAJ5.0A
- D24: value SS36(F) -> SMAJ5.0A
- D25, D5: value SS36(F) -> AZ23C16; footprint Diode_SMD:D_SMA -> Package_TO_SOT_SMD:SOT-23
- D26: value SMAJ12A -> AZ23C16; footprint Diode_SMD:D_SMA -> Package_TO_SOT_SMD:SOT-23
- D27: value SMAJ12A -> SS36(F)
- D28, D39, D40, D8: value AZ23C16 -> SS36(F); footprint Package_TO_SOT_SMD:SOT-23 -> Diode_SMD:D_SMA
- D30: value SMAJ9.0A -> Green; footprint Diode_SMD:D_SMA -> LED_SMD:LED_0603_1608Metric
- D31, D43, D47, D53: value SS36(F) -> Red; footprint Diode_SMD:D_SMA -> LED_SMD:LED_0603_1608Metric
- D33, D34, D37, D38: value SMAJ5.0A -> AZ23C16; footprint Diode_SMD:D_SMA -> Package_TO_SOT_SMD:SOT-23
- D35, D36: value SMAJ5.0A -> SS36(F)
- D57, D58: value SS36(F) -> SMAJ12A
- D7: value SMAJ24A -> SS36(F)
- D9: value SMAJ9.0A -> Red; footprint Diode_SMD:D_SMA -> LED_SMD:LED_0603_1608Metric
- Q1: value STN2610D -> BC847; footprint Package_TO_SOT_SMD:TO-252-2 -> Package_TO_SOT_SMD:SOT-23
- Q5: value BC847 -> STN2610D; footprint Package_TO_SOT_SMD:SOT-23 -> Package_TO_SOT_SMD:TO-252-2
- R10, R81, R82, R9: value 1M -> 15k
- R100, R137, R31, R67, R99: value 1M -> 390k
- R101, R153, R154, R49, R83: value 1M -> 100k
- R104, R133, R156, R39, R61, R86: value 100k -> 1M
- R105, R13, R131, R132, R14, R15, R159, R41, R62, R87: value 390k -> 1M
- R106, R134, R160, R42, R88: value 390k -> 33k
- R107, R89: value 15k -> 1M
- R108, R90: value 15k -> 33k
- R109, R110, R55, R56, R91, R92: value 33mR -> 390k; footprint Resistor_SMD:R_1206_3216Metric -> Resistor_SMD:R_0603_1608Metric
- R111, R112, R140, R22, R93, R94: value 100k -> 10k
- R113, R114, R141, R142, R23, R24, R95, R96: value 390k -> 33mR; footprint Resistor_SMD:R_0603_1608Metric -> Resistor_SMD:R_1206_3216Metric
- R116, R26, R59, R60, R98: value 390k -> 100k
- R117, R118, R119, R121, R27, R28, R29: value 1M -> 150R
- R120, R122, R147, R148, R30, R75, R76: value 100k -> 150R
- R123, R124, R51, R52, R77, R78: value 390k -> 150R
- R125, R126, R161, R162, R20, R7: value 15k -> 390k
- R127, R128, R5: value 33mR -> 15k; footprint Resistor_SMD:R_1206_3216Metric -> Resistor_SMD:R_0603_1608Metric
- R136, R16, R64: value 1M -> 33k
- R138, R32, R43, R68, R79, R8: value 100k -> 390k
- R139, R45, R46: value 1M -> 10k
- R143, R144, R35, R36: value 15k -> 100k
- R145, R146: value 33mR -> 150R; footprint Resistor_SMD:R_1206_3216Metric -> Resistor_SMD:R_0603_1608Metric
- R151, R57, R58: value 100k -> 15k
- R152, R33, R34, R6: value 390k -> 15k
- R158, R18, R40, R66: value 100k -> 33k
- R163, R164, R21: value 33mR -> 10k; footprint Resistor_SMD:R_1206_3216Metric -> Resistor_SMD:R_0603_1608Metric
- R165, R166, R48: value 100k -> 33mR; footprint Resistor_SMD:R_0603_1608Metric -> Resistor_SMD:R_1206_3216Metric
- R37, R38: value 33mR -> 1M; footprint Resistor_SMD:R_1206_3216Metric -> Resistor_SMD:R_0603_1608Metric
- R47: value 1M -> 33mR; footprint Resistor_SMD:R_0603_1608Metric -> Resistor_SMD:R_1206_3216Metric
- R53, R54: value 15k -> 150R
- R69, R70: value 390k -> 10k
- R71, R72: value 15k -> 33mR; footprint Resistor_SMD:R_0603_1608Metric -> Resistor_SMD:R_1206_3216Metric
- R73, R74: value 33mR -> 100k; footprint Resistor_SMD:R_1206_3216Metric -> Resistor_SMD:R_0603_1608Metric
- U3: value LM324 -> ESP32-S2-WROVER; footprint Package_SO:TSSOP-14_4.4x5mm_P0.65mm -> RF_Module:ESP32-S2-WROVER
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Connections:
- net /Dual output7/Iset1 renamed /DC Output channels/D_{Out}36
- net /Dual output7/Iset2 renamed /DC Output channels/D_{Out}37
- C10 pad 1: Net-(U3A--) -> Net-(U4B--)
- C10 pad 2: Net-(C10-Pad2) -> /DC Output channels/A_{In}3
- C11 pad 1: Net-(U3C-+) -> Net-(U4D--)
- C11 pad 2: Net-(C11-Pad2) -> /DC Output channels/A_{In}4
- C12 pad 1: Net-(U3D--) -> +12V
- C12 pad 2: /Dual output/Isns2 -> GND
- C13 pad 1: Net-(U4A--) -> Net-(U5A--)
- C14 pad 1: Net-(U4C-+) -> Net-(U5C-+)
- C15 pad 1: Net-(U4B--) -> Net-(U5B--)
- C15 pad 2: /Dual output1/Isns1 -> /DC Output channels/A_{In}3
- C16 pad 1: Net-(U4D--) -> Net-(U5D--)
- C16 pad 2: /Dual output1/Isns2 -> /DC Output channels/A_{In}4
- C18 pad 1: Net-(U5A--) -> Net-(U6A--)
- C19 pad 1: Net-(U5C-+) -> Net-(U6C-+)
- C20 pad 1: Net-(U5B--) -> Net-(U6B--)
- C20 pad 2: /Dual output2/Isns1 -> /DC Output channels/A_{In}1
- C21 pad 1: Net-(U5D--) -> Net-(U6D--)
- C21 pad 2: /Dual output2/Isns2 -> /DC Output channels/A_{In}2
- C23 pad 1: Net-(U6A--) -> Net-(U7A--)
- C24 pad 1: Net-(U6C-+) -> Net-(U7C-+)
- C25 pad 1: Net-(U6B--) -> Net-(U7B--)
- C25 pad 2: /Dual output3/Isns1 -> /DC Output channels/A_{In}1
- C26 pad 1: Net-(U6D--) -> Net-(U7D--)
- C26 pad 2: /Dual output3/Isns2 -> /DC Output channels/A_{In}2
- C28 pad 1: Net-(U7A--) -> Net-(U9A--)
- C30 pad 2: /Dual output6/Isns1 -> /DC Output channels/A_{In}1
- C31 pad 2: /Dual output6/Isns2 -> /DC Output channels/A_{In}2
- C33 pad 1: Net-(U10A--) -> Net-(U8A--)
- C34 pad 1: Net-(U11C-+) -> Net-(U10C-+)
- C35 pad 2: /Dual output5/Isns1 -> /DC Output channels/A_{In}1
- C36 pad 2: /Dual output5/Isns2 -> /DC Output channels/A_{In}2
- C38 pad 1: Net-(U13A--) -> Net-(U10A--)
- C39 pad 1: Net-(U13C-+) -> Net-(U9C-+)
- C40 pad 1: Net-(U13B--) -> Net-(U9B--)
- C40 pad 2: /Dual output4/Isns1 -> /DC Output channels/A_{In}1
- C41 pad 1: Net-(U13D--) -> Net-(U9D--)
- C41 pad 2: /Dual output4/Isns2 -> /DC Output channels/A_{In}2
- C43 pad 1: Net-(U14A--) -> Net-(U11A--)
- C44 pad 1: Net-(U15C-+) -> Net-(U11C-+)
- C45 pad 1: Net-(U15B--) -> Net-(U10B--)
- C45 pad 2: /Dual output8/Isns1 -> /DC Output channels/A_{In}1
- C46 pad 1: Net-(U15D--) -> Net-(U10D--)
- C46 pad 2: /Dual output8/Isns2 -> /DC Output channels/A_{In}2
- C48 pad 1: Net-(U16A--) -> Net-(U12A--)
- C49 pad 1: Net-(U16C-+) -> Net-(U12C-+)
- C50 pad 1: Net-(U16B--) -> Net-(U13B--)
- C50 pad 2: /Dual output7/Isns1 -> /DC Output channels/A_{In}1
- C51 pad 1: Net-(U16D--) -> Net-(U13D--)
- C51 pad 2: /Dual output7/Isns2 -> /DC Output channels/A_{In}2
- C8 pad 1: Net-(U3B--) -> Net-(U4A--)
- C8 pad 2: /Dual output/Isns1 -> Net-(C8-Pad2)
- C9 pad 1: +12V -> Net-(U4C-+)
- C9 pad 2: GND -> Net-(C9-Pad2)
- D10 pad 1: Net-(D10-K) -> /DC Output channels/D_{Out}9
- D10 pad 2: +24V -> Net-(D10-A)
- D11 pad 1: /Dual output/O2+ -> /DC Output channels/D_{Out}10
- D11 pad 2: /Dual output/O2+ -> Net-(D11-A)
- D12 pad 1: /Dual output1/O1+ -> /DC Output channels/D_{Out}11
- D12 pad 2: /Dual output1/O1- -> Net-(D12-A)
- D13 pad 1: /Dual output1/O2+ -> /DC Output channels/5V output #2/O1+
- D13 pad 2: /Dual output1/O2+ -> /DC Output channels/5V output #2/O1-
- D14 pad 1: Net-(Q11-G) -> /DC Output channels/5V output #2/O2+
- D14 pad 2: /Dual output1/O1+ -> /DC Output channels/5V output #2/O2+
- D15 pad 1: Net-(Q12-G) -> Net-(Q11-G)
- D15 pad 2: /Dual output1/O2+ -> /DC Output channels/5V output #3/O1+
- D16 pad 1: /Dual output8/O2+ -> Net-(Q12-G)
- D16 pad 2: /Dual output8/O2+ -> /DC Output channels/5V output #3/O2+
- D17 pad 2: +12V -> +5V
- D18 pad 2: +12V -> +5V
- D19 pad 1: /Dual output2/O1+ -> /DC Output channels/D_{Out}14
- D19 pad 2: /Dual output2/O1- -> Net-(D19-A)
- D20 pad 1: /Dual output2/O2+ -> /DC Output channels/D_{Out}15
- D20 pad 2: /Dual output2/O2+ -> Net-(D20-A)
- D21 pad 1: Net-(Q17-G) -> /DC Output channels/D_{Out}16
- D21 pad 2: /Dual output2/O1+ -> Net-(D21-A)
- D22 pad 1: Net-(Q18-G) -> /DC Output channels/D_{Out}17
- D22 pad 2: /Dual output2/O2+ -> Net-(D22-A)
- D23 pad 1: /Dual output7/O1+ -> /DC Output channels/5V output #3/O1+
- D23 pad 2: /Dual output7/O1- -> /DC Output channels/5V output #3/O1-
- D24 pad 1: Net-(D24-K) -> /DC Output channels/5V output #3/O2+
- D24 pad 2: +12V -> /DC Output channels/5V output #3/O2+
- D25 pad 1: Net-(D25-K) -> Net-(Q17-G)
- D25 pad 2: +12V -> /DC Output channels/24V output #1/O1+
- D26 pad 1: /Dual output3/O1+ -> Net-(Q18-G)
- D26 pad 2: /Dual output3/O1- -> /DC Output channels/24V output #1/O2+
- D27 pad 1: /Dual output3/O2+ -> Net-(D27-K)
- D27 pad 2: /Dual output3/O2+ -> +24V
- D28 pad 1: Net-(Q23-G) -> Net-(D28-K)
- D28 pad 2: /Dual output3/O1+ -> +24V
- D29 pad 1: Net-(Q24-G) -> /DC Output channels/D_{Out}20
- D29 pad 2: /Dual output3/O2+ -> Net-(D29-A)
- D30 pad 1: /Dual output7/O2+ -> /DC Output channels/D_{Out}21
- D30 pad 2: /Dual output7/O2+ -> Net-(D30-A)
- D31 pad 1: Net-(D31-K) -> /DC Output channels/D_{Out}22
- D31 pad 2: +12V -> Net-(D31-A)
- D32 pad 1: Net-(D32-K) -> /DC Output channels/D_{Out}23
- D32 pad 2: +12V -> Net-(D32-A)
- D33 pad 1: /Dual output6/O1+ -> Net-(Q23-G)
- D33 pad 2: /Dual output6/O1- -> /DC Output channels/12V output #1/O1+
- D34 pad 1: /Dual output6/O2+ -> Net-(Q24-G)
- D34 pad 2: /Dual output6/O2+ -> /DC Output channels/12V output #1/O2+
- D35 pad 1: /Dual output5/O1+ -> Net-(D35-K)
- D35 pad 2: /Dual output5/O1- -> +12V
- D36 pad 1: /Dual output5/O2+ -> Net-(D36-K)
- D36 pad 2: /Dual output5/O2+ -> +12V
- D37 pad 1: /Dual output4/O1+ -> Net-(Q35-G)
- D37 pad 2: /Dual output4/O1- -> /DC Output channels/5V output #1/O1+
- D38 pad 1: /Dual output4/O2+ -> Net-(Q36-G)
- D38 pad 2: /Dual output4/O2+ -> /DC Output channels/5V output #1/O2+
- D39 pad 1: Net-(Q29-G) -> Net-(D39-K)
- D39 pad 2: /Dual output6/O1+ -> +5V
- D40 pad 1: Net-(Q30-G) -> Net-(D40-K)
- D40 pad 2: /Dual output6/O2+ -> +5V
- D41 pad 1: Net-(Q47-G) -> /DC Output channels/D_{Out}4
- D41 pad 2: /Dual output8/O1+ -> Net-(D41-A)
- D42 pad 1: Net-(D42-K) -> /DC Output channels/D_{Out}5
- D42 pad 2: +5V -> Net-(D42-A)
- D43 pad 1: Net-(D43-K) -> /DC Output channels/D_{Out}2
- D43 pad 2: +5V -> Net-(D43-A)
- D44 pad 1: Net-(Q35-G) -> /DC Output channels/D_{Out}3
- D44 pad 2: /Dual output5/O1+ -> Net-(D44-A)
- D45 pad 1: Net-(Q36-G) -> /DC Output channels/D_{Out}26
- D45 pad 2: /Dual output5/O2+ -> Net-(D45-A)
- D46 pad 1: Net-(Q48-G) -> /DC Output channels/D_{Out}27
- D46 pad 2: /Dual output8/O2+ -> Net-(D46-A)
- D47 pad 1: Net-(D47-K) -> /DC Output channels/D_{Out}28
- D47 pad 2: +5V -> Net-(D47-A)
- D48 pad 1: Net-(D48-K) -> /DC Output channels/D_{Out}29
- D48 pad 2: +5V -> Net-(D48-A)
- D49 pad 1: Net-(Q41-G) -> Net-(Q29-G)
- D49 pad 2: /Dual output4/O1+ -> /DC Output channels/12V output #2/O1+
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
